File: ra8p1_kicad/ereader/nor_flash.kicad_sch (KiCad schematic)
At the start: 17 parts, among them U15 S28HL01GTFPBHI030

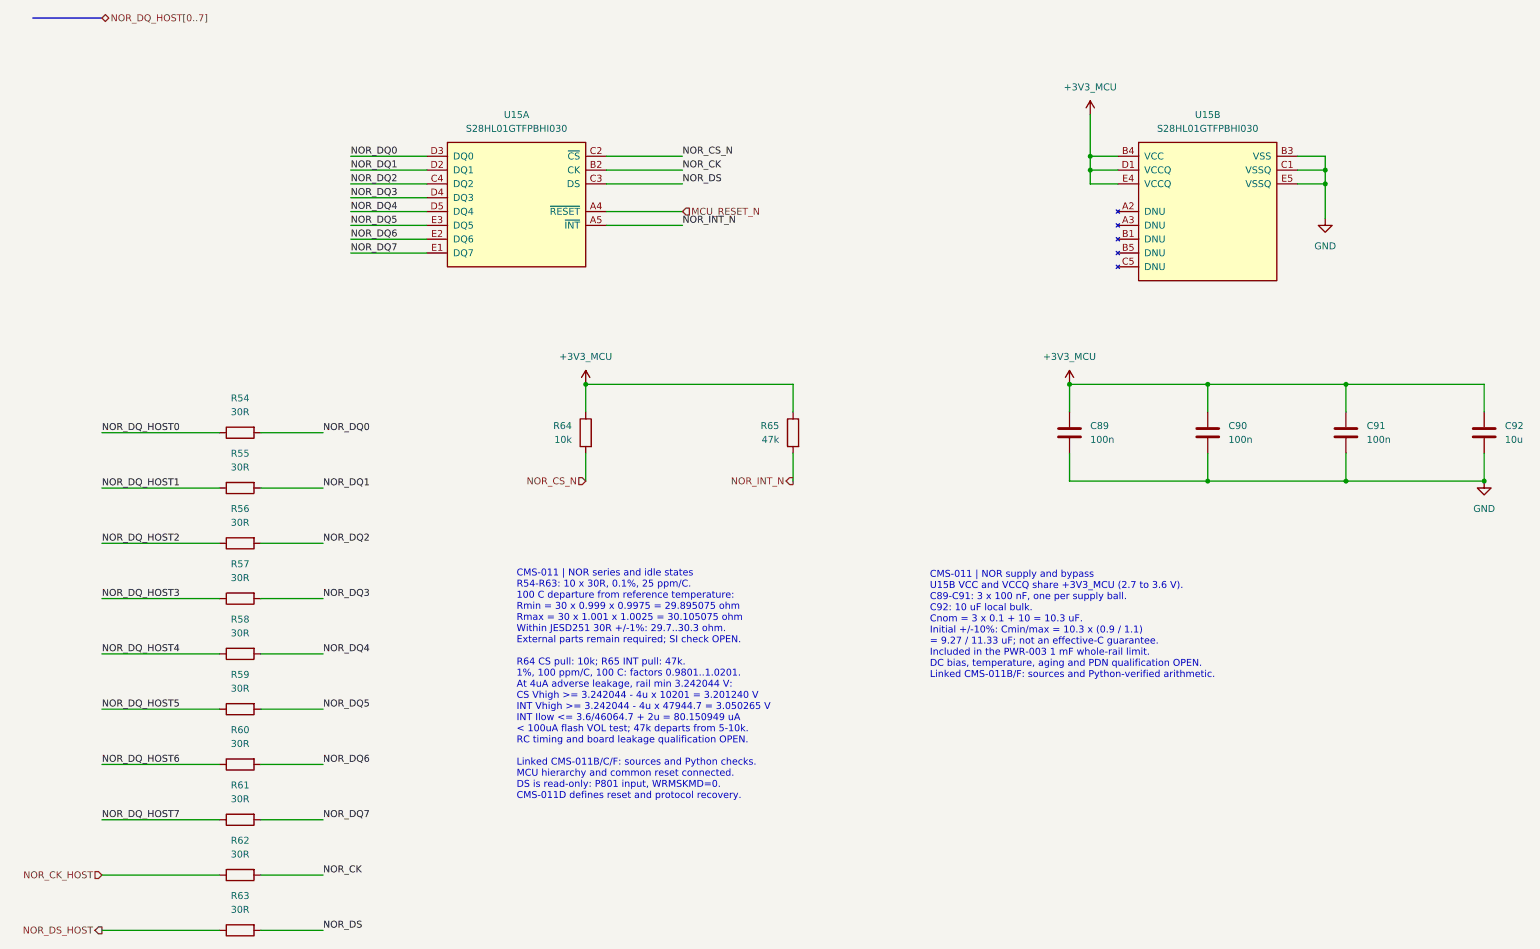
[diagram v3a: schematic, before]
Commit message: wip(hardware): preserve schematic cleanup and CEU host ports
Checkpoint cosmetic cleanup across the schematic hierarchy and eleven parallel-camera host ports. Refresh the complete 13-page PDF. All 334 existing net partitions and 271 component records match the prior CEU checkpoint; all 128 ERC identities remain unchanged. Electrical design is incomplete; this is a WIP checkpoint for #821 and #841.
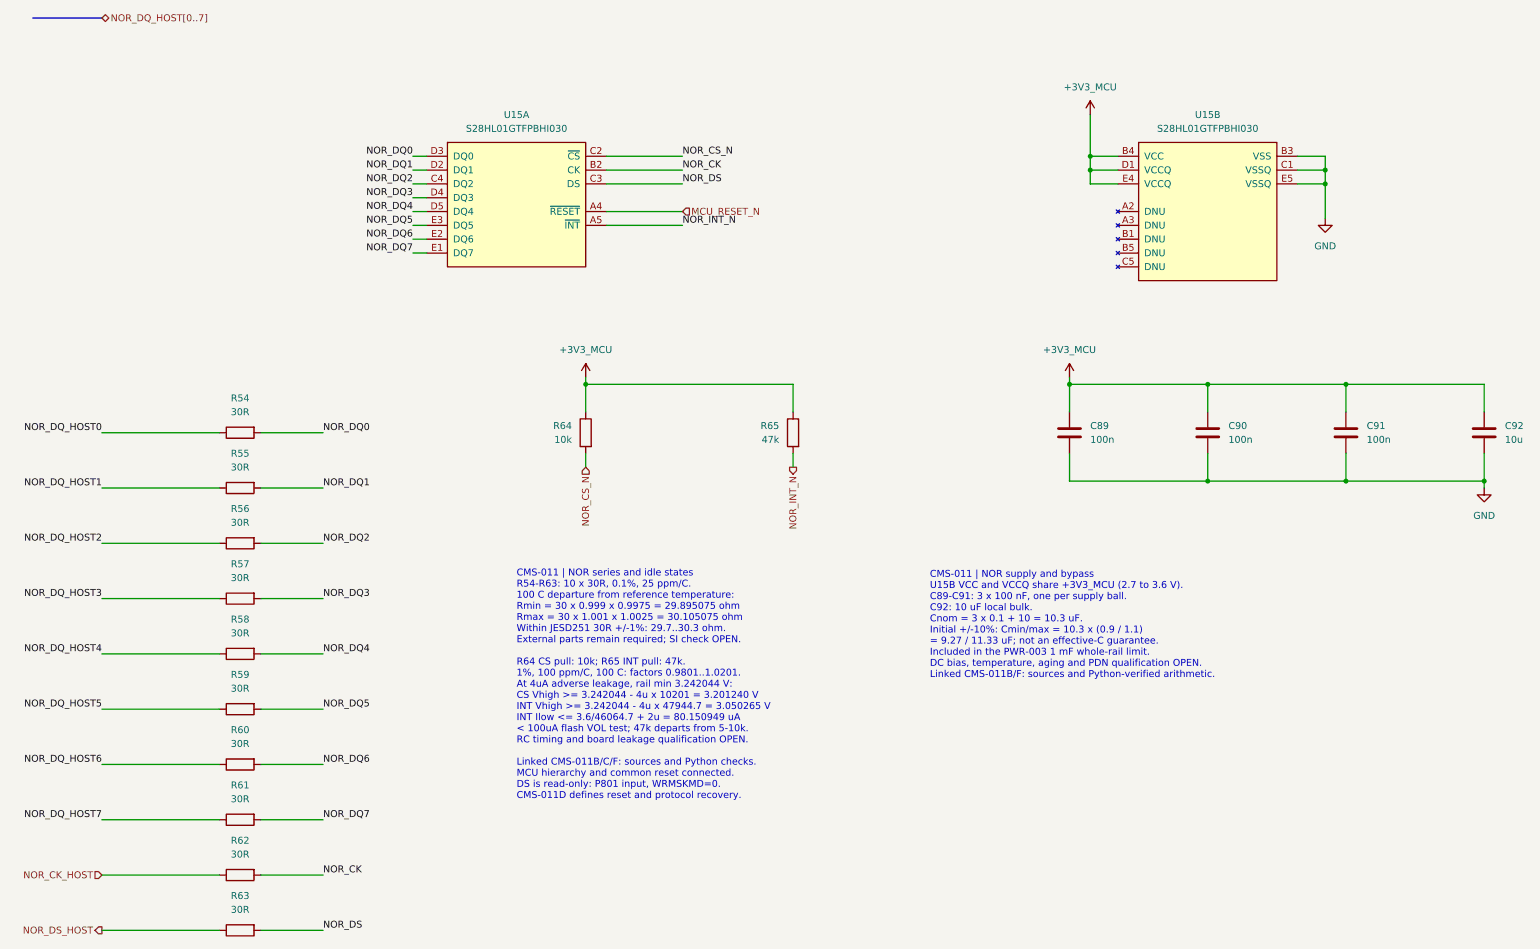
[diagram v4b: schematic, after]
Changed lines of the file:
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@@
 	(wire
 		(pts
-			(xy 121.92 99.06) (xy 135.89 99.06)
+			(xy 133.35 99.06) (xy 135.89 99.06)
 		)
 		(stroke
@@
 	(wire
 		(pts
+			(xy 330.2 149.86) (xy 330.2 148.59)
+		)
+		(stroke
+			(width 0)
+			(type default)
+		)
+	)
+	(wire
+		(pts
 			(xy 168.91 93.98) (xy 182.88 93.98)
 		)
@@
 	(wire
 		(pts
-			(xy 121.92 106.68) (xy 135.89 106.68)
+			(xy 133.35 106.68) (xy 135.89 106.68)
+		)
+		(stroke
+			(width 0)
+			(type default)
+		)
+	)
+	(wire
+		(pts
+			(xy 165.1 129.54) (xy 165.1 130.81)
 		)
 		(stroke
@@
 		)
 	)
+	(wire
+		(pts
+			(xy 254 129.54) (xy 254 130.81)
+		)
+		(stroke
+			(width 0)
+			(type default)
+		)
+	)
 	(bus
 		(pts
@@
 	(wire
 		(pts
-			(xy 121.92 96.52) (xy 135.89 96.52)
+			(xy 133.35 96.52) (xy 135.89 96.52)
 		)
 		(stroke
@@
 	(wire
 		(pts
-			(xy 203.2 143.51) (xy 203.2 148.59)
+			(xy 203.2 143.51) (xy 203.2 146.05)
 		)
 		(stroke
@@
 	(wire
 		(pts
-			(xy 121.92 91.44) (xy 135.89 91.44)
+			(xy 133.35 91.44) (xy 135.89 91.44)
 		)
 		(stroke
@@
 	(wire
 		(pts
-			(xy 121.92 104.14) (xy 135.89 104.14)
+			(xy 133.35 104.14) (xy 135.89 104.14)
 		)
 		(stroke
@@
 	(wire
 		(pts
-			(xy 165.1 143.51) (xy 165.1 148.59)
+			(xy 165.1 143.51) (xy 165.1 146.05)
 		)
 		(stroke
@@
 	(wire
 		(pts
-			(xy 121.92 93.98) (xy 135.89 93.98)
+			(xy 133.35 93.98) (xy 135.89 93.98)
 		)
 		(stroke
@@
 	(wire
 		(pts
-			(xy 121.92 101.6) (xy 135.89 101.6)
+			(xy 133.35 101.6) (xy 135.89 101.6)
 		)
 		(stroke
@@
 	(wire
 		(pts
-			(xy 121.92 88.9) (xy 135.89 88.9)
+			(xy 133.35 88.9) (xy 135.89 88.9)
 		)
 		(stroke
@@
 	)
 	(label "NOR_DQ2"
-		(at 121.92 93.98 0)
+		(at 133.35 93.98 180)
 		(effects
 			(font
 				(size 1.27 1.27)
 			)
-			(justify left bottom)
+			(justify right bottom)
 		)
 	)
@@
 	)
 	(label "NOR_DQ_HOST5"
-		(at 76.2 190.5 0)
+		(at 76.2 190.5 180)
 		(effects
 			(font
 				(size 1.27 1.27)
 			)
-			(justify left bottom)
+			(justify right bottom)
 		)
 	)
@@
 	)
 	(label "NOR_DQ3"
-		(at 121.92 96.52 0)
+		(at 133.35 96.52 180)
 		(effects
 			(font
 				(size 1.27 1.27)
 			)
-			(justify left bottom)
+			(justify right bottom)
 		)
 	)
@@
 	)
 	(label "NOR_DQ_HOST0"
-		(at 76.2 139.7 0)
+		(at 76.2 139.7 180)
 		(effects
 			(font
 				(size 1.27 1.27)
 			)
-			(justify left bottom)
+			(justify right bottom)
 		)
 	)
@@
 	)
 	(label "NOR_DQ_HOST1"
-		(at 76.2 149.86 0)
+		(at 76.2 149.86 180)
 		(effects
 			(font
 				(size 1.27 1.27)
 			)
-			(justify left bottom)
+			(justify right bottom)
 		)
 	)
 	(label "NOR_DQ_HOST6"
-		(at 76.2 200.66 0)
+		(at 76.2 200.66 180)
 		(effects
 			(font
 				(size 1.27 1.27)
 			)
-			(justify left bottom)
+			(justify right bottom)
 		)
 	)
 	(label "NOR_DQ0"
-		(at 121.92 88.9 0)
+		(at 133.35 88.9 180)
 		(effects
 			(font
 				(size 1.27 1.27)
 			)
-			(justify left bottom)
+			(justify right bottom)
 		)
 	)
 	(label "NOR_DQ_HOST2"
-		(at 76.2 160.02 0)
+		(at 76.2 160.02 180)
 		(effects
 			(font
 				(size 1.27 1.27)
 			)
-			(justify left bottom)
+			(justify right bottom)
 		)
 	)
@@
 	)
 	(label "NOR_DQ5"
-		(at 121.92 101.6 0)
+		(at 133.35 101.6 180)
 		(effects
 			(font
 				(size 1.27 1.27)
 			)
-			(justify left bottom)
+			(justify right bottom)
 		)
 	)
 	(label "NOR_DQ1"
-		(at 121.92 91.44 0)
+		(at 133.35 91.44 180)
 		(effects
 			(font
 				(size 1.27 1.27)
 			)
-			(justify left bottom)
+			(justify right bottom)
 		)
 	)
 	(label "NOR_DQ_HOST3"
-		(at 76.2 170.18 0)
+		(at 76.2 170.18 180)
 		(effects
 			(font
 				(size 1.27 1.27)
 			)
-			(justify left bottom)
+			(justify right bottom)
 		)
 	)
@@
 	)
 	(label "NOR_DQ6"
-		(at 121.92 104.14 0)
+		(at 133.35 104.14 180)
 		(effects
 			(font
 				(size 1.27 1.27)
 			)
-			(justify left bottom)
+			(justify right bottom)
 		)
 	)
 	(label "NOR_DQ7"
-		(at 121.92 106.68 0)
+		(at 133.35 106.68 180)
 		(effects
 			(font
 				(size 1.27 1.27)
 			)
-			(justify left bottom)
+			(justify right bottom)
 		)
 	)
 	(label "NOR_DQ_HOST4"
-		(at 76.2 180.34 0)
+		(at 76.2 180.34 180)
 		(effects
 			(font
 				(size 1.27 1.27)
 			)
-			(justify left bottom)
+			(justify right bottom)
 		)
 	)
 	(label "NOR_DQ4"
-		(at 121.92 99.06 0)
+		(at 133.35 99.06 180)
 		(effects
 			(font
 				(size 1.27 1.27)
 			)
-			(justify left bottom)
+			(justify right bottom)
 		)
 	)
@@
 	)
 	(label "NOR_DQ_HOST7"
-		(at 76.2 210.82 0)
+		(at 76.2 210.82 180)
 		(effects
 			(font
 				(size 1.27 1.27)
 			)
-			(justify left bottom)
+			(justify right bottom)
 		)
 	)
@@
 	(hierarchical_label "NOR_INT_N"
 		(shape output)
-		(at 203.2 148.59 180)
+		(at 203.2 146.05 270)
 		(effects
 			(font
@@
 	(hierarchical_label "NOR_CS_N"
 		(shape input)
-		(at 165.1 148.59 180)
+		(at 165.1 146.05 270)
 		(effects
 			(font
@@
 	(symbol
 		(lib_id "power:VCC")
-		(at 165.1 130.81 0)
+		(at 165.1 129.54 0)
 		(unit 1)
 		(body_style 1)
@@
 		(fields_autoplaced yes)
 		(property "Reference" "#PWR0154"
-			(at 165.1 134.62 0)
+			(at 165.1 133.35 0)
 			(hide yes)
 			(show_name no)
@@
 		)
 		(property "Value" "+3V3_MCU"
-			(at 165.1 125.73 0)
+			(at 165.1 124.46 0)
 			(show_name no)
 			(do_not_autoplace no)
@@
 		)
 		(property "Footprint" ""
-			(at 165.1 130.81 0)
+			(at 165.1 129.54 0)
 			(hide yes)
 			(show_name no)
@@
 		)
 		(property "Datasheet" ""
-			(at 165.1 130.81 0)
+			(at 165.1 129.54 0)
 			(hide yes)
 			(show_name no)
@@
 		)
 		(property "Description" "Power symbol creates a global label with name \"VCC\""
-			(at 165.1 130.81 0)
+			(at 165.1 129.54 0)
 			(hide yes)
 			(show_name no)
@@
 	(symbol
 		(lib_id "power:GND")
-		(at 330.2 148.59 0)
+		(at 330.2 149.86 0)
 		(unit 1)
 		(body_style 1)
@@
 		(fields_autoplaced yes)
 		(property "Reference" "#PWR0153"
-			(at 330.2 154.94 0)
+			(at 330.2 156.21 0)
 			(hide yes)
 			(show_name no)
@@
 		)
 		(property "Value" "GND"
-			(at 330.2 153.67 0)
+			(at 330.2 154.94 0)
 			(show_name no)
 			(do_not_autoplace no)
@@
 		)
 		(property "Footprint" ""
-			(at 330.2 148.59 0)
+			(at 330.2 149.86 0)
 			(hide yes)
 			(show_name no)
@@
 		)
 		(property "Datasheet" ""
-			(at 330.2 148.59 0)
+			(at 330.2 149.86 0)
 			(hide yes)
 			(show_name no)
@@
 		)
 		(property "Description" "Power symbol creates a global label with name \"GND\" , ground"
-			(at 330.2 148.59 0)
+			(at 330.2 149.86 0)
 			(hide yes)
 			(show_name no)
@@
 	(symbol
 		(lib_id "power:VCC")
-		(at 254 130.81 0)
+		(at 254 129.54 0)
 		(unit 1)
 		(body_style 1)
@@
 		(fields_autoplaced yes)
 		(property "Reference" "#PWR0152"
-			(at 254 134.62 0)
+			(at 254 133.35 0)
 			(hide yes)
 			(show_name no)
@@
 		)
 		(property "Value" "+3V3_MCU"
-			(at 254 125.73 0)
+			(at 254 124.46 0)
 			(show_name no)
 			(do_not_autoplace no)
@@
 		)
 		(property "Footprint" ""
-			(at 254 130.81 0)
+			(at 254 129.54 0)
 			(hide yes)
 			(show_name no)
@@
 		)
 		(property "Datasheet" ""
-			(at 254 130.81 0)
+			(at 254 129.54 0)
 			(hide yes)
 			(show_name no)
@@
 		)
 		(property "Description" "Power symbol creates a global label with name \"VCC\""
-			(at 254 130.81 0)
+			(at 254 129.54 0)
 			(hide yes)
 			(show_name no)
